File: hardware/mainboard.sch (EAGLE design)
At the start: 79 parts, among them IC1 ATMEGA328, IC10 HM628512A_DIL32, IC11 HM628512A_DIL32, IC12 7805TV, IC13 DS1210, IC14 6N138, IC3 TLC074, IC4 74HCT04N, IC5 74HC238N, IC6 74HCT573N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

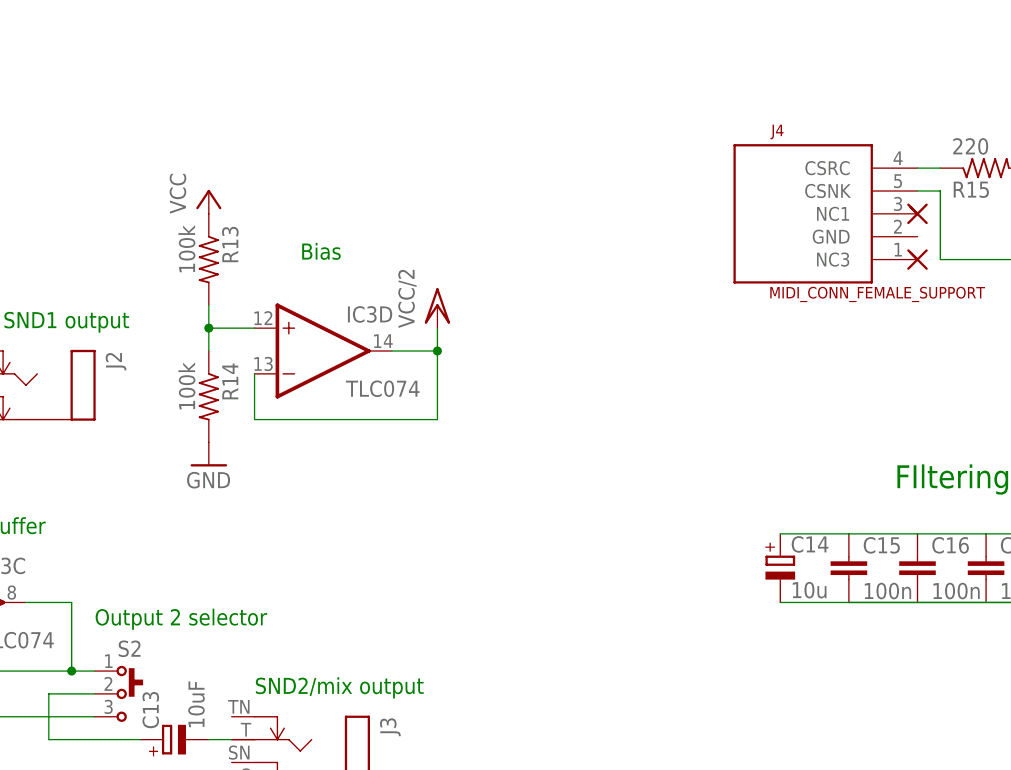
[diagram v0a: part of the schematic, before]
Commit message: main board: add decoupling to bias voltage divider
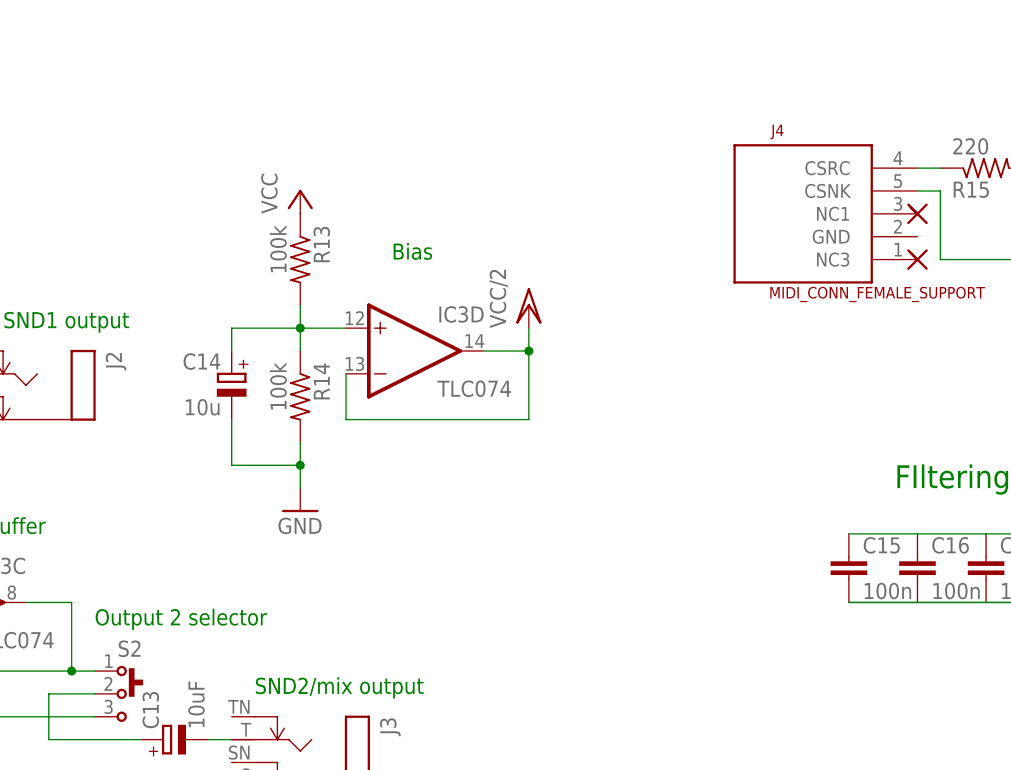
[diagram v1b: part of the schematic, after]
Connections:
- net N$28: now also C14.+
- net VCC: no longer C14.+
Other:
- moved on the sheet: C14, IC3D, R13, R14
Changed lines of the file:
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@@
 <?xml version="1.0" encoding="utf-8"?>
 <!DOCTYPE eagle SYSTEM "eagle.dtd">
-<eagle version="7.3.0">
+<eagle version="7.4.0">
 <drawing>
 <settings>
@@
 <text x="228.6" y="-132.08" size="2.54" layer="91" font="vector">(c) 2014-2015 Johan Fjeldtvedt</text>
 <text x="233.68" y="-142.24" size="2.54" layer="91" font="vector">NESIZER synthesizer board</text>
-<text x="50.8" y="-71.12" size="1.778" layer="91">Bias</text>
+<text x="60.96" y="-71.12" size="1.778" layer="91">Bias</text>
 </plain>
 <instances>
@@
 <instance part="R19" gate="G$1" x="289.56" y="-71.12" rot="MR270"/>
 <instance part="GND19" gate="1" x="193.04" y="-30.48"/>
-<instance part="C14" gate="G$1" x="104.14" y="-104.14"/>
+<instance part="C14" gate="G$1" x="43.18" y="-83.82" rot="MR0"/>
 <instance part="GND6" gate="1" x="-48.26" y="-93.98"/>
 <instance part="GND21" gate="1" x="-48.26" y="-142.24"/>
 <instance part="IC3" gate="C" x="12.7" y="-109.22"/>
-<instance part="IC3" gate="D" x="53.34" y="-81.28"/>
-<instance part="R14" gate="G$1" x="40.64" y="-86.36" rot="R270"/>
-<instance part="R13" gate="G$1" x="40.64" y="-71.12" rot="R270"/>
-<instance part="P+12" gate="VCC" x="40.64" y="-63.5"/>
-<instance part="GND7" gate="1" x="40.64" y="-93.98"/>
-<instance part="P+17" gate="G$1" x="66.04" y="-76.2"/>
+<instance part="IC3" gate="D" x="63.5" y="-81.28"/>
+<instance part="R14" gate="G$1" x="50.8" y="-86.36" rot="R270"/>
+<instance part="R13" gate="G$1" x="50.8" y="-71.12" rot="R270"/>
+<instance part="P+12" gate="VCC" x="50.8" y="-63.5"/>
+<instance part="GND7" gate="1" x="50.8" y="-99.06"/>
+<instance part="P+17" gate="G$1" x="76.2" y="-76.2"/>
 <instance part="P+18" gate="G$1" x="-22.86" y="-139.7" rot="R180"/>
 <instance part="P+19" gate="G$1" x="-22.86" y="-91.44" rot="R180"/>
@@
 <pinref part="C25" gate="G$1" pin="2"/>
 <wire x1="180.34" y1="-109.22" x2="187.96" y2="-109.22" width="0.1524" layer="91"/>
-<pinref part="C14" gate="G$1" pin="-"/>
-<wire x1="104.14" y1="-109.22" x2="111.76" y2="-109.22" width="0.1524" layer="91"/>
 </segment>
 <segment>
@@
 <pinref part="R14" gate="G$1" pin="2"/>
 <pinref part="GND7" gate="1" pin="GND"/>
+<wire x1="50.8" y1="-96.52" x2="50.8" y2="-93.98" width="0.1524" layer="91"/>
+<pinref part="C14" gate="G$1" pin="-"/>
+<wire x1="50.8" y1="-93.98" x2="50.8" y2="-91.44" width="0.1524" layer="91"/>
+<wire x1="43.18" y1="-88.9" x2="43.18" y2="-93.98" width="0.1524" layer="91"/>
+<wire x1="43.18" y1="-93.98" x2="50.8" y2="-93.98" width="0.1524" layer="91"/>
+<junction x="50.8" y="-93.98"/>
 </segment>
 </net>
@@
 <pinref part="C24" gate="G$1" pin="1"/>
 <wire x1="187.96" y1="-101.6" x2="180.34" y2="-101.6" width="0.1524" layer="91"/>
-<pinref part="C14" gate="G$1" pin="+"/>
-<wire x1="111.76" y1="-101.6" x2="104.14" y2="-101.6" width="0.1524" layer="91"/>
 </segment>
 <segment>
@@
 <pinref part="R14" gate="G$1" pin="1"/>
 <pinref part="R13" gate="G$1" pin="2"/>
-<wire x1="40.64" y1="-81.28" x2="40.64" y2="-78.74" width="0.1524" layer="91"/>
+<wire x1="50.8" y1="-81.28" x2="50.8" y2="-78.74" width="0.1524" layer="91"/>
 <pinref part="IC3" gate="D" pin="+IN"/>
-<wire x1="40.64" y1="-78.74" x2="40.64" y2="-76.2" width="0.1524" layer="91"/>
-<wire x1="45.72" y1="-78.74" x2="40.64" y2="-78.74" width="0.1524" layer="91"/>
-<junction x="40.64" y="-78.74"/>
+<wire x1="50.8" y1="-78.74" x2="50.8" y2="-76.2" width="0.1524" layer="91"/>
+<wire x1="55.88" y1="-78.74" x2="50.8" y2="-78.74" width="0.1524" layer="91"/>
+<junction x="50.8" y="-78.74"/>
+<pinref part="C14" gate="G$1" pin="+"/>
+<wire x1="50.8" y1="-78.74" x2="43.18" y2="-78.74" width="0.1524" layer="91"/>
+<wire x1="43.18" y1="-78.74" x2="43.18" y2="-81.28" width="0.1524" layer="91"/>
 </segment>
 </net>
@@
 <segment>
 <pinref part="IC3" gate="D" pin="-IN"/>
-<wire x1="45.72" y1="-83.82" x2="45.72" y2="-88.9" width="0.1524" layer="91"/>
-<wire x1="45.72" y1="-88.9" x2="66.04" y2="-88.9" width="0.1524" layer="91"/>
-<wire x1="66.04" y1="-88.9" x2="66.04" y2="-81.28" width="0.1524" layer="91"/>
+<wire x1="55.88" y1="-83.82" x2="55.88" y2="-88.9" width="0.1524" layer="91"/>
+<wire x1="55.88" y1="-88.9" x2="76.2" y2="-88.9" width="0.1524" layer="91"/>
+<wire x1="76.2" y1="-88.9" x2="76.2" y2="-81.28" width="0.1524" layer="91"/>
 <pinref part="IC3" gate="D" pin="OUT"/>
-<wire x1="66.04" y1="-81.28" x2="60.96" y2="-81.28" width="0.1524" layer="91"/>
-<wire x1="66.04" y1="-81.28" x2="66.04" y2="-78.74" width="0.1524" layer="91"/>
+<wire x1="76.2" y1="-81.28" x2="71.12" y2="-81.28" width="0.1524" layer="91"/>
+<wire x1="76.2" y1="-81.28" x2="76.2" y2="-78.74" width="0.1524" layer="91"/>
 <pinref part="P+17" gate="G$1" pin="VCC/2"/>
-<junction x="66.04" y="-81.28"/>
-</segment>
-<segment>
+<junction x="76.2" y="-81.28"/>
+</segment>
+<segment>

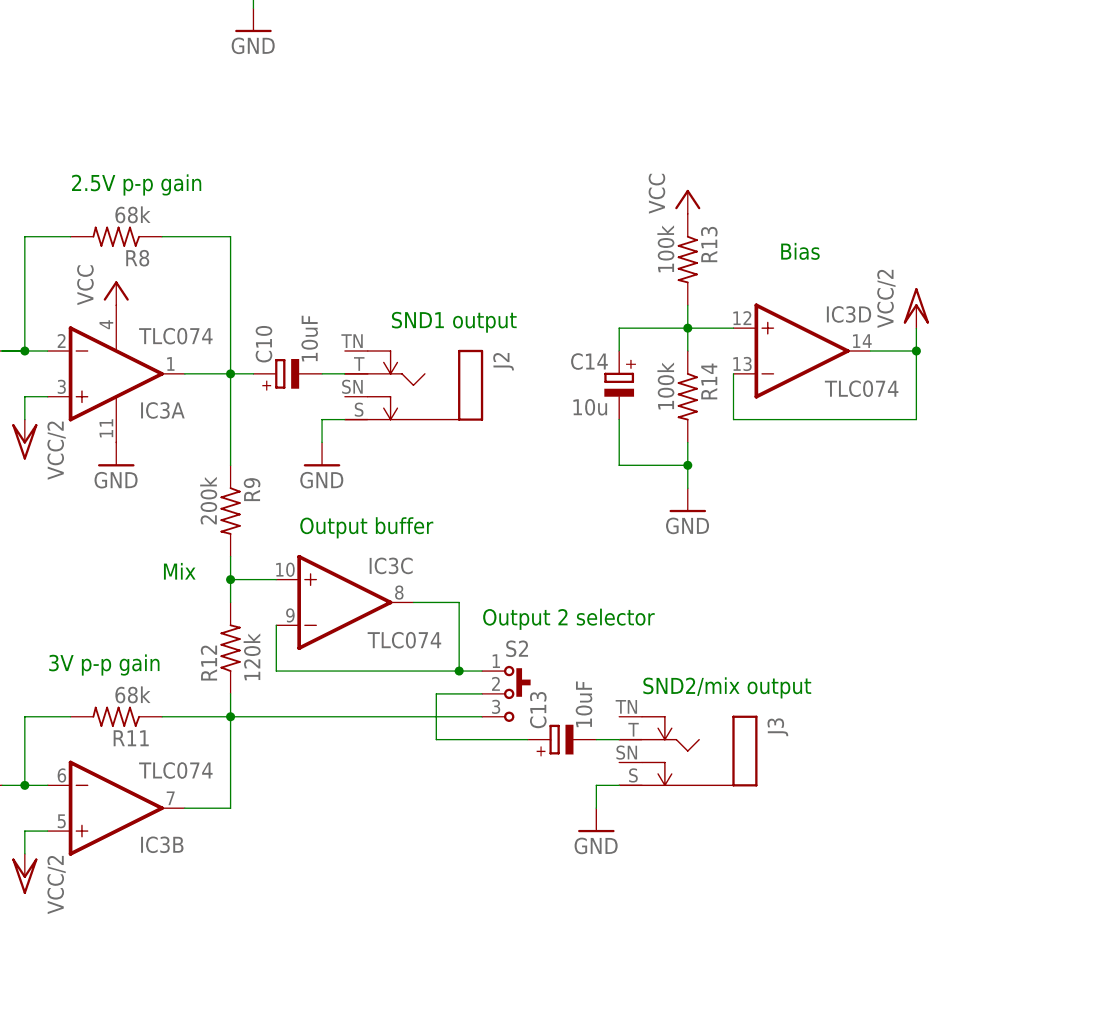
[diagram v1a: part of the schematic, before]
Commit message: replace mix buffer with inverting mixer to reduce crosstalk
scm
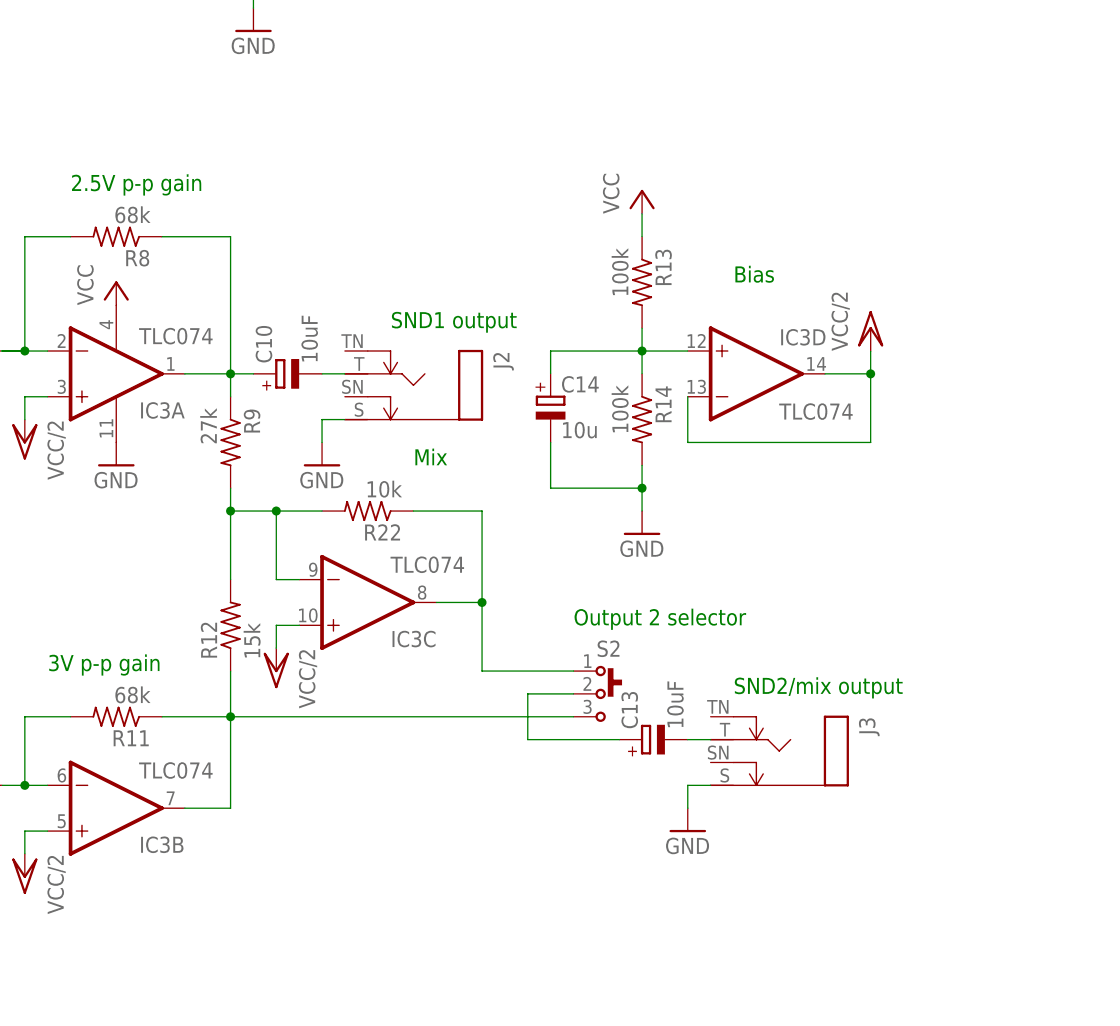
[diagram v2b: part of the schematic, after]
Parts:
- added R22: 10k, rcl:R-US_0207/7
- R12: value 120k -> 15k
- R9: value 200k -> 27k
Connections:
- net N$14: now also IC3C.-IN, R22.2; no longer IC3C.+IN
- net N$26: now also R22.1; no longer IC3C.-IN
- net VCC/2: now also IC3C.+IN
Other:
- note removed: "Output buffer"
- moved on the sheet: C13, C14, IC3C, IC3D, J3, R12, R13, R14, R9, S2
